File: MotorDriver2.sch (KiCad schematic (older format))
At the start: 38 parts, among them J20 43045-0802, J21 53426-0410, U41 MAX40056FAUA+, U42 DRV8312DDWR, U43 MAX40056FAUA+, U44 MIC2090-2YM5-TR

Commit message: PVT
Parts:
- C166: renamed from C174; footprint Capacitor-Chip:C_CHIP_1608_Reflow -> Capacitor-Chip:C_CHIP_1005_Hand_NoSilk; PartName GRM188R61E105KA12D -> TMK105BJ105MV-F
- C167: renamed from C175; PartName C1005X5R1V105K050BE -> TMK105BJ105MV-F
- C168: renamed from C176; PartName C1005X5R1V105K050BE -> TMK105BJ105MV-F
- C169: renamed from C177; footprint Capacitor-Chip:C_CHIP_1608_Reflow -> Capacitor-Chip:C_CHIP_1005_Hand_NoSilk; PartName GRM188R61E105KA12D -> TMK105BJ105MV-F
- C170: renamed from C178; footprint Capacitor-Chip:C_CHIP_1608_Reflow -> Capacitor-Chip:C_CHIP_1005_Hand_NoSilk; PartName GRM188R61E105KA12D -> TMK105BJ105MV-F
- C171: renamed from C179; footprint Capacitor-Chip:C_CHIP_1608_Reflow -> Capacitor-Chip:C_CHIP_1005_Hand_NoSilk; PartName GRM188R61E105KA12D -> TMK105BJ105MV-F
- C173: renamed from C181; PartName C1005X5R1V105K050BE -> TMK105BJ105MV-F
- C174: renamed from C182; PartName C1005X5R1V105K050BE -> TMK105BJ105MV-F
- C182: renamed from C190; PartName C1005X5R1V105K050BE -> TMK105BJ105MV-F
- R94: renamed from R109; value 2m -> 3m; PartName PMR18EZPJV2L0 -> PMR18EZPFV3L00
- R95: renamed from R110; value 2m -> 3m; PartName PMR18EZPJV2L0 -> PMR18EZPFV3L00
- renumbered C180 to C172, C183 to C175, C184 to C176, C185 to C177, C186 to C178, C187 to C179, C188 to C180, C189 to C181, L16 to L12, L17 to L13, L18 to L14, R105 to R90, R106 to R91, R107 to R92, R108 to R93, R111 to R96, R112 to R97, RA21 to RA22, RA22 to RA23, RA23 to RA24, U41 to U38, U42 to U39, U43 to U40, U44 to U41

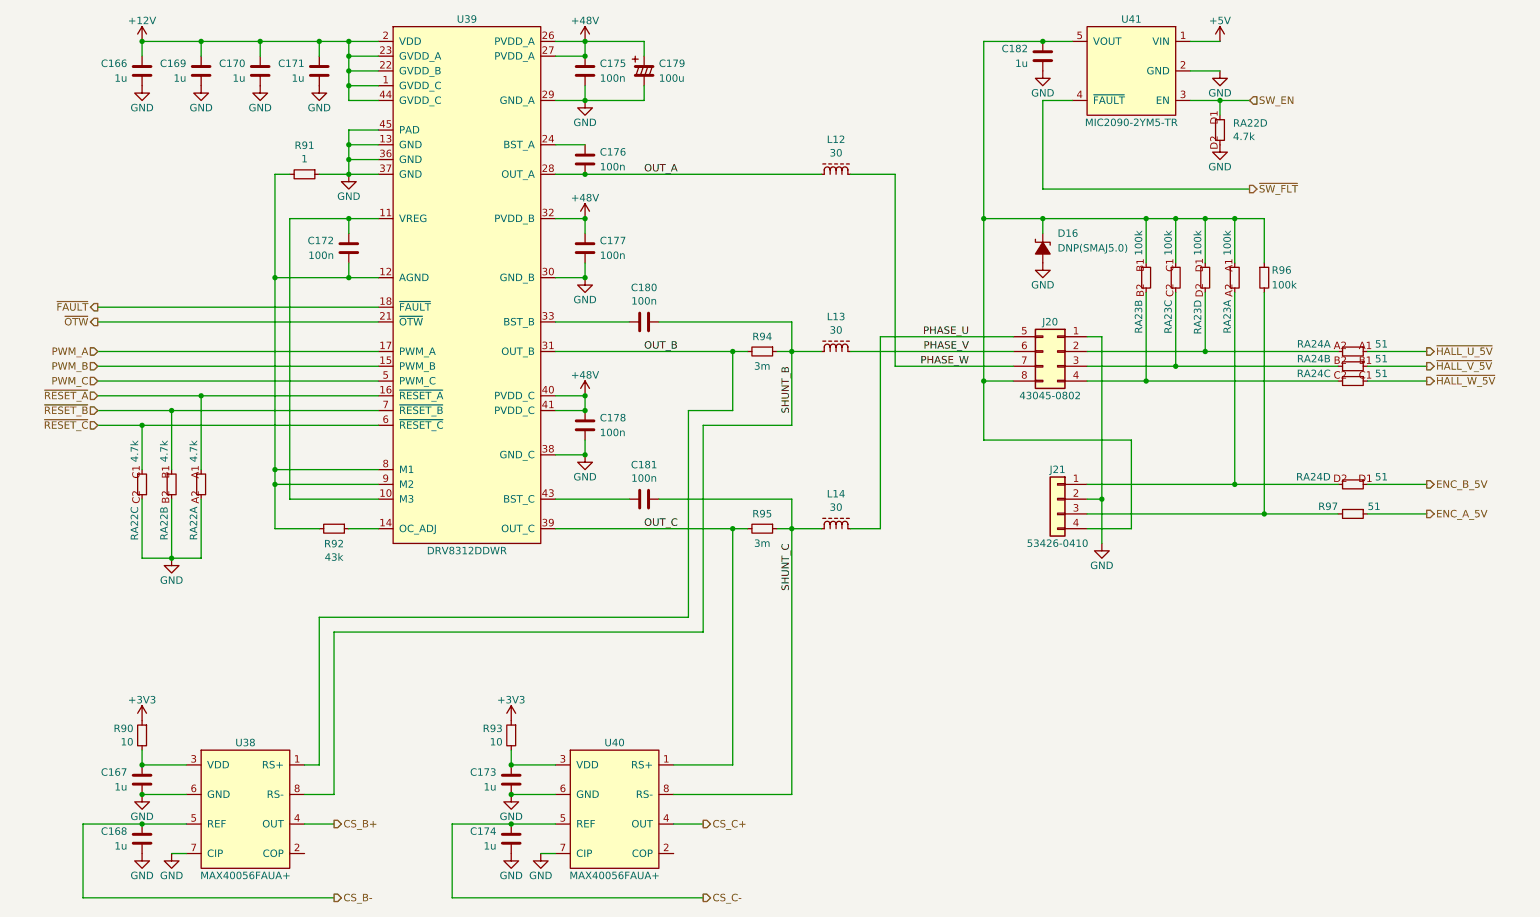
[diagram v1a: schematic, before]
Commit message: SBUにTVSダイオードを追加
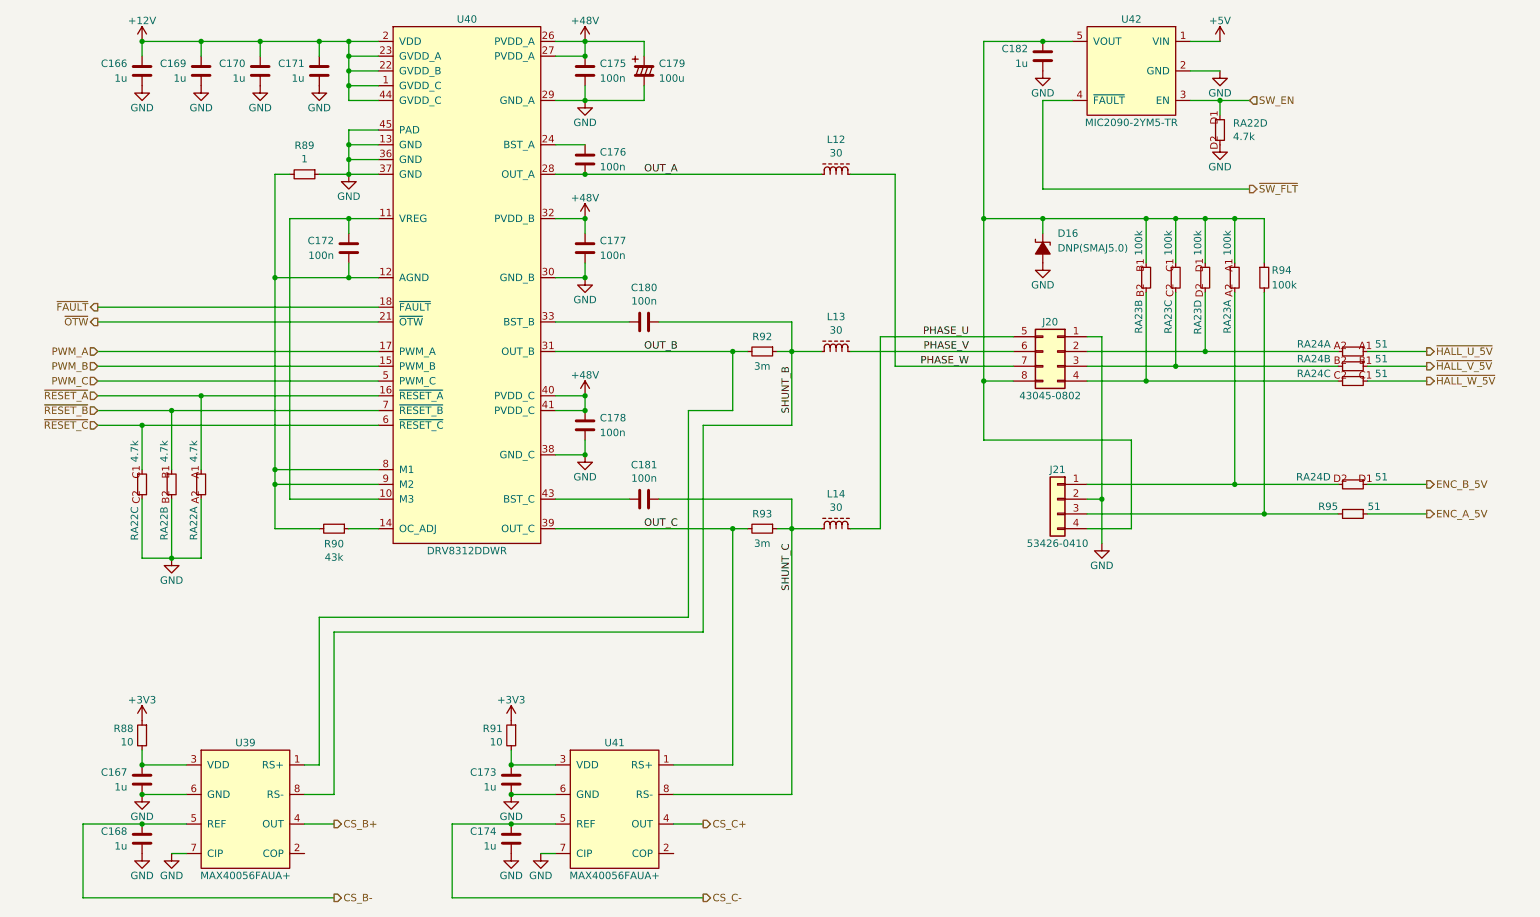
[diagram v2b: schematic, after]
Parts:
- renumbered R90 to R88, R91 to R89, R92 to R90, R93 to R91, R94 to R92, R95 to R93, R96 to R94, R97 to R95, U38 to U39, U39 to U40, U40 to U41, U41 to U42
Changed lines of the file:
@@
 AR Path="/5F235A43/5E5B7AF9" Ref="U?"  Part="1"
 AR Path="/5F237486/5E5B7AF9" Ref="U?"  Part="1"
-AR Path="/5F259EEE/5E5B7AF9" Ref="U39"  Part="1"
-F 0 "U39" H 4000 4850 50  0000 C CNN
+AR Path="/5F259EEE/5E5B7AF9" Ref="U40"  Part="1"
+F 0 "U40" H 4000 4850 50  0000 C CNN
 F 1 "DRV8312DDWR" H 4000 1250 50  0000 C CNN
 F 2 "IC-SOP:HTSSOP44-W6.1_EP4.31x8.26" H 4000 3000 50  0001 C CNN
@@
 AR Path="/5F235A43/5E5B7BE9" Ref="R?"  Part="1"
 AR Path="/5F237486/5E5B7BE9" Ref="R?"  Part="1"
-AR Path="/5F259EEE/5E5B7BE9" Ref="R91"  Part="1"
-F 0 "R91" V 2705 2200 50  0000 C CNN
+AR Path="/5F259EEE/5E5B7BE9" Ref="R89"  Part="1"
+F 0 "R89" V 2705 2200 50  0000 C CNN
 F 1 "1" V 2796 2200 50  0000 C CNN
 F 2 "Resistor-Chip:R_CHIP_1005_Hand_NoSilk" V 2950 2100 50  0001 C CNN
@@
 AR Path="/5F235A43/5E5B7BF3" Ref="R?"  Part="1"
 AR Path="/5F237486/5E5B7BF3" Ref="R?"  Part="1"
-AR Path="/5F259EEE/5E5B7BF3" Ref="R92"  Part="1"
-F 0 "R92" V 3203 4600 50  0000 C CNN
+AR Path="/5F259EEE/5E5B7BF3" Ref="R90"  Part="1"
+F 0 "R90" V 3203 4600 50  0000 C CNN
 F 1 "43k" V 3294 4600 50  0000 C CNN
 F 2 "Resistor-Chip:R_CHIP_1005_Hand_NoSilk" V 3150 4500 50  0001 C CNN
@@
 AR Path="/5F235A43/5E5B7C08" Ref="R?"  Part="1"
 AR Path="/5F237486/5E5B7C08" Ref="R?"  Part="1"
-AR Path="/5F259EEE/5E5B7C08" Ref="R95"  Part="1"
-F 0 "R95" V 5900 4600 50  0000 C CNN
+AR Path="/5F259EEE/5E5B7C08" Ref="R93"  Part="1"
+F 0 "R93" V 5900 4600 50  0000 C CNN
 F 1 "3m" V 6100 4600 50  0000 C CNN
 F 2 "Resistor-Chip:R_CHIP_3216_Reflow" V 6050 4500 50  0001 C CNN
@@
 AR Path="/5F235A43/5E5B7C15" Ref="R?"  Part="1"
 AR Path="/5F237486/5E5B7C15" Ref="R?"  Part="1"
-AR Path="/5F259EEE/5E5B7C15" Ref="R94"  Part="1"
-F 0 "R94" V 5900 3400 50  0000 C CNN
+AR Path="/5F259EEE/5E5B7C15" Ref="R92"  Part="1"
+F 0 "R92" V 5900 3400 50  0000 C CNN
 F 1 "3m" V 6100 3400 50  0000 C CNN
 F 2 "Resistor-Chip:R_CHIP_3216_Reflow" V 6050 3300 50  0001 C CNN
@@
 AR Path="/5F235278/5F12DD03" Ref="U?"  Part="1"
 AR Path="/5F235A43/5F12DD03" Ref="U?"  Part="1"
-AR Path="/5F259EEE/5F12DD03" Ref="U41"  Part="1"
-F 0 "U41" H 8500 1850 50  0000 C CNN
+AR Path="/5F259EEE/5F12DD03" Ref="U42"  Part="1"
+F 0 "U42" H 8500 1850 50  0000 C CNN
 F 1 "MIC2090-2YM5-TR" H 8500 1150 50  0000 C CNN
 F 2 "IC-SOT:SOT23-5" H 8500 1500 50  0001 C CNN
@@
 AR Path="/5F235A43/5F4A623B" Ref="U?"  Part="1"
 AR Path="/5F237486/5F4A623B" Ref="U?"  Part="1"
-AR Path="/5F259EEE/5F4A623B" Ref="U38"  Part="1"
-F 0 "U38" H 2500 6950 50  0000 C CNN
+AR Path="/5F259EEE/5F4A623B" Ref="U39"  Part="1"
+F 0 "U39" H 2500 6950 50  0000 C CNN
 F 1 "MAX40056FAUA+" H 2500 6050 50  0000 C CNN
 F 2 "IC-SOP:MSOP8" H 2500 6500 50  0001 C CNN
@@
 AR Path="/5F235A43/5F4A6241" Ref="U?"  Part="1"
 AR Path="/5F237486/5F4A6241" Ref="U?"  Part="1"
-AR Path="/5F259EEE/5F4A6241" Ref="U40"  Part="1"
-F 0 "U40" H 5000 6950 50  0000 C CNN
+AR Path="/5F259EEE/5F4A6241" Ref="U41"  Part="1"
+F 0 "U41" H 5000 6950 50  0000 C CNN
 F 1 "MAX40056FAUA+" H 5000 6050 50  0000 C CNN
 F 2 "IC-SOP:MSOP8" H 5000 6500 50  0001 C CNN
@@
 AR Path="/5F235A43/5F4A62A7" Ref="R?"  Part="1"
 AR Path="/5F237486/5F4A62A7" Ref="R?"  Part="1"
-AR Path="/5F259EEE/5F4A62A7" Ref="R90"  Part="1"
-F 0 "R90" H 1858 6046 50  0000 L CNN
+AR Path="/5F259EEE/5F4A62A7" Ref="R88"  Part="1"
+F 0 "R88" H 1858 6046 50  0000 L CNN
 F 1 "10" H 1858 5955 50  0000 L CNN
 F 2 "Resistor-Chip:R_CHIP_1005_Hand_NoSilk" V 1850 5900 50  0001 C CNN
@@
 AR Path="/5F235A43/5F4A62AD" Ref="R?"  Part="1"
 AR Path="/5F237486/5F4A62AD" Ref="R?"  Part="1"
-AR Path="/5F259EEE/5F4A62AD" Ref="R93"  Part="1"
-F 0 "R93" H 4358 6046 50  0000 L CNN
+AR Path="/5F259EEE/5F4A62AD" Ref="R91"  Part="1"
+F 0 "R91" H 4358 6046 50  0000 L CNN
 F 1 "10" H 4358 5955 50  0000 L CNN
 F 2 "Resistor-Chip:R_CHIP_1005_Hand_NoSilk" V 4350 5900 50  0001 C CNN
@@
 P 9400 2900
 AR Path="/5F235A43/5E96246C" Ref="R?"  Part="1"
-AR Path="/5F259EEE/5E96246C" Ref="R96"  Part="1"
-F 0 "R96" H 9450 2950 50  0000 L CNN
+AR Path="/5F259EEE/5E96246C" Ref="R94"  Part="1"
+F 0 "R94" H 9450 2950 50  0000 L CNN
 F 1 "100k" H 9450 2850 50  0000 L CNN
 F 2 "Resistor-Chip:R_CHIP_1005_Hand_NoSilk" V 9450 2800 50  0001 C CNN
@@
 P 10000 4500
 AR Path="/5F235A43/5E9984BF" Ref="R?"  Part="1"
-AR Path="/5F259EEE/5E9984BF" Ref="R97"  Part="1"
-F 0 "R97" V 9950 4400 50  0000 R CNN
+AR Path="/5F259EEE/5E9984BF" Ref="R95"  Part="1"
+F 0 "R95" V 9950 4400 50  0000 R CNN
 F 1 "51" V 9950 4600 50  0000 L CNN
 F 2 "Resistor-Chip:R_CHIP_1005_Hand_NoSilk" V 10050 4400 50  0001 C CNN
